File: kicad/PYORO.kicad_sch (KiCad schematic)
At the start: 69 parts, among them J1 BM06B-SRSS-TBLFSN, J2 Conn_01x04_Pin, J3 BM06B-SRSS-TBLFSN, Q1 TEFT4300, Q2 TEFT4300, Q3 TEFT4300, Q4 TEFT4300, Q5 NMOS, Q6 NMOS, Q7 NMOS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

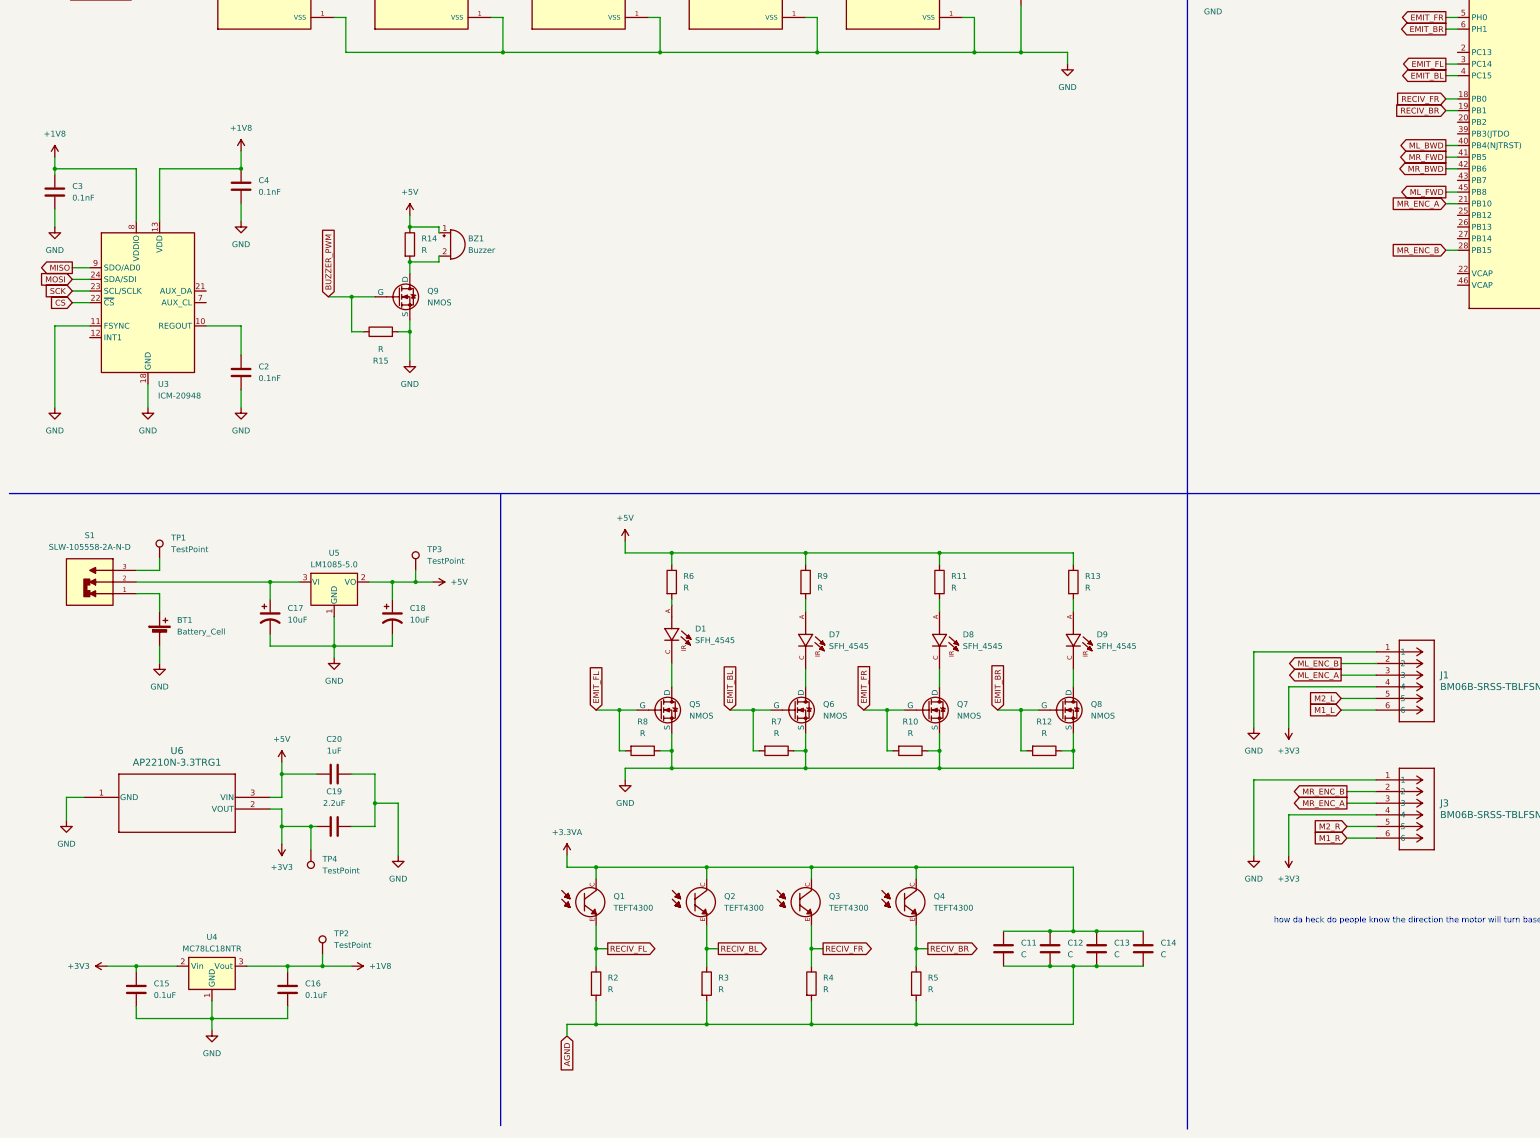
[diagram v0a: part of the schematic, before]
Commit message: Started LEDs for the extra GPIO pins
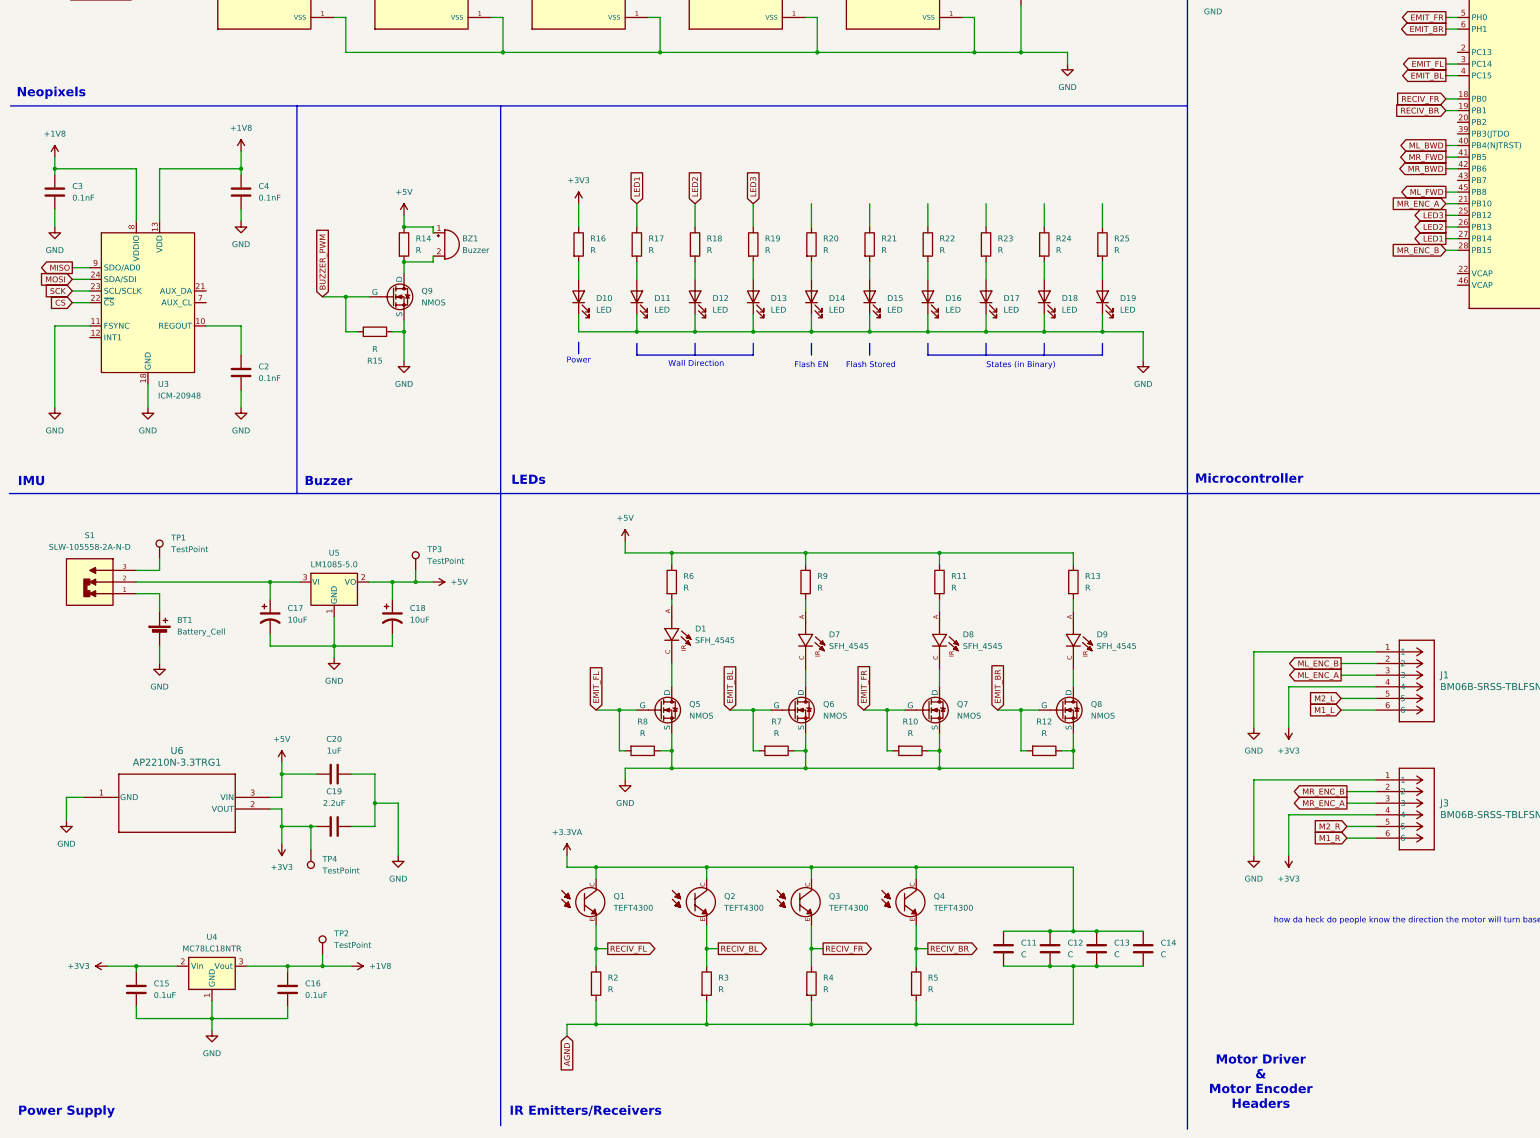
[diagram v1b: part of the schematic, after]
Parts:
- added D10, D11, D12, D13, D14, D15, D16, D17, D18, D19: LED, symbol Device:LED
- added R16, R17, R18, R19, R20, R21, R22, R23, R24, R25: R, symbol Device:R
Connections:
- net +3V3: now also R16.1
- net GND: now also D10.1 (K), D11.1 (K), D12.1 (K), D13.1 (K), D14.1 (K), D15.1 (K), D16.1 (K), D17.1 (K), D18.1 (K), D19.1 (K)
- net LED3: now reaches U1.25 (PB12)
- net LED3: now also R19.1
- net LED2: now reaches U1.26 (PB13)
- net LED2: now also R18.1
- net LED1: now reaches U1.27 (PB14)
- net LED1: now also R17.1
- new net: D17.2 (A), R23.2
- new net: D11.2 (A), R17.2
- new net: D14.2 (A), R20.2
- new net: D12.2 (A), R18.2
- new net: D18.2 (A), R24.2
- new net: D10.2 (A), R16.2
- new net: D19.2 (A), R25.2
- new net: D15.2 (A), R21.2
- new net: D13.2 (A), R19.2
- new net: D16.2 (A), R22.2
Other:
- note added: "Buzzer"
- note added: "Flash EN"
- note added: "Flash Stored"
- note added: "IMU"
- note added: "IR Emitters/Receivers"
- note added: "LEDs"
- note added: "Microcontroller"
- note added: "Motor Driver & Motor Encoder Headers"
- note added: "Neopixels"
- note added: "Power"
- note added: "Power Supply"
- note added: "States (in Binary)"
- note added: "Wall Direction"
- moved on the sheet: BZ1, C4, Q9, R14, R15

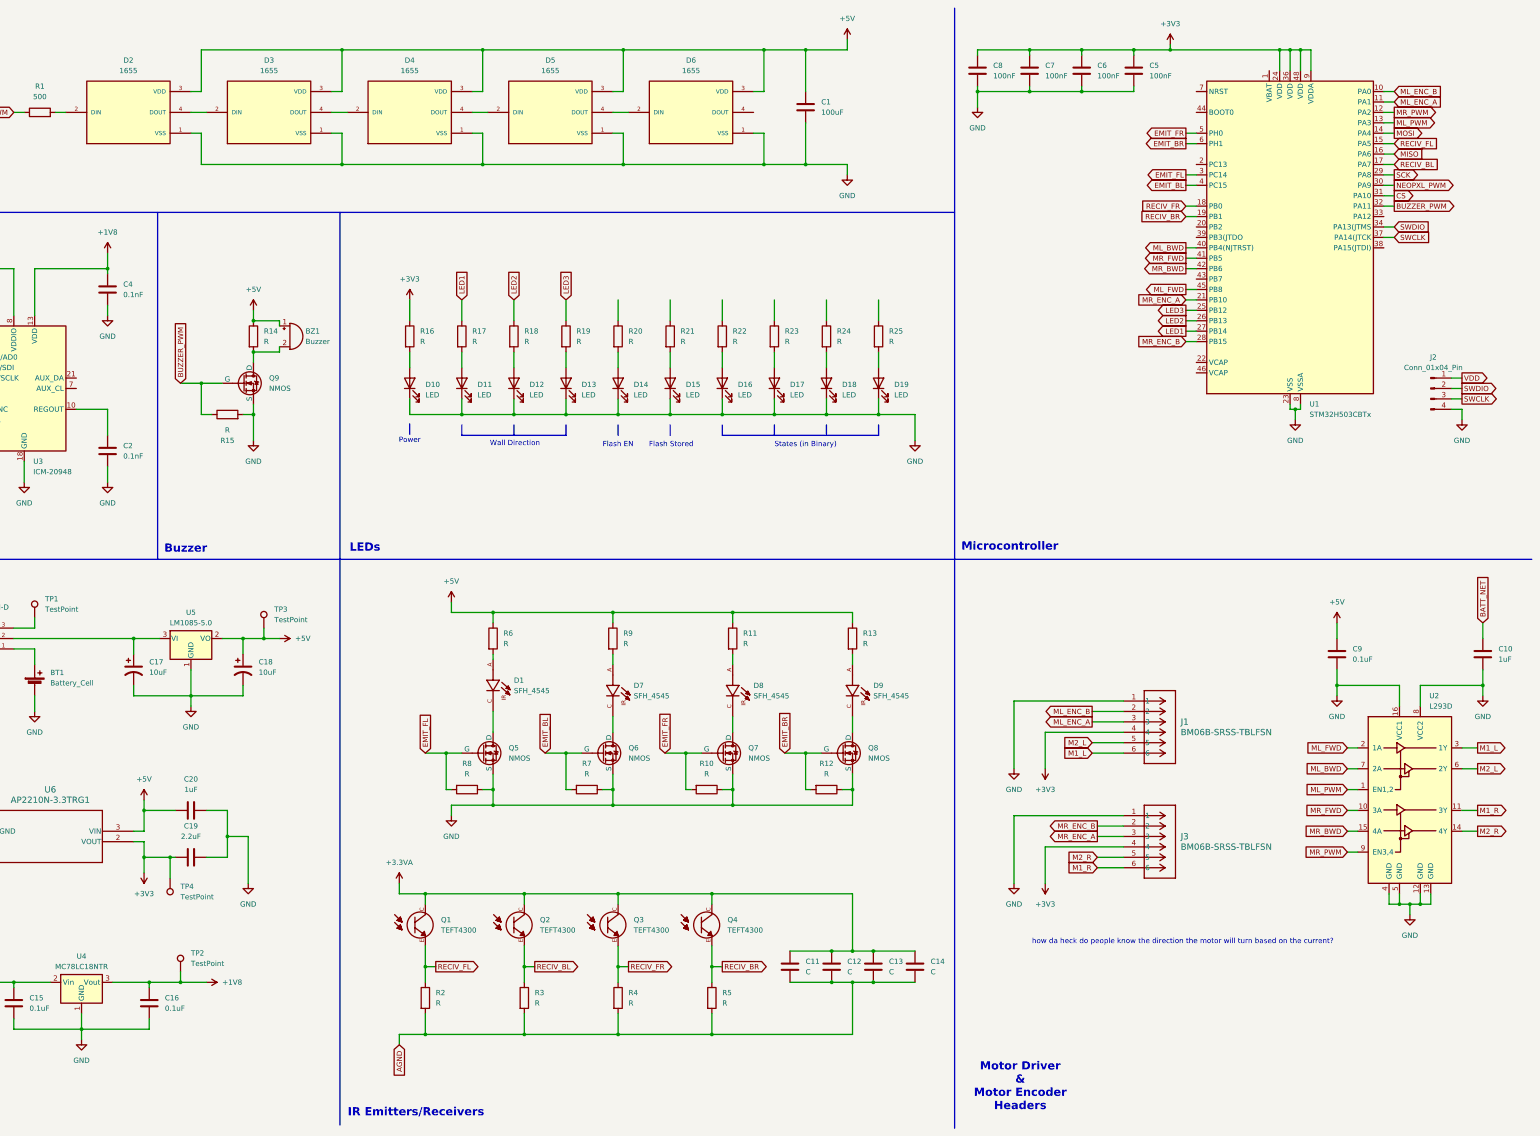
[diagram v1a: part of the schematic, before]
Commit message: Added new test points, updated missing Capacitor and Resistor values, fix MCU power supply scheme
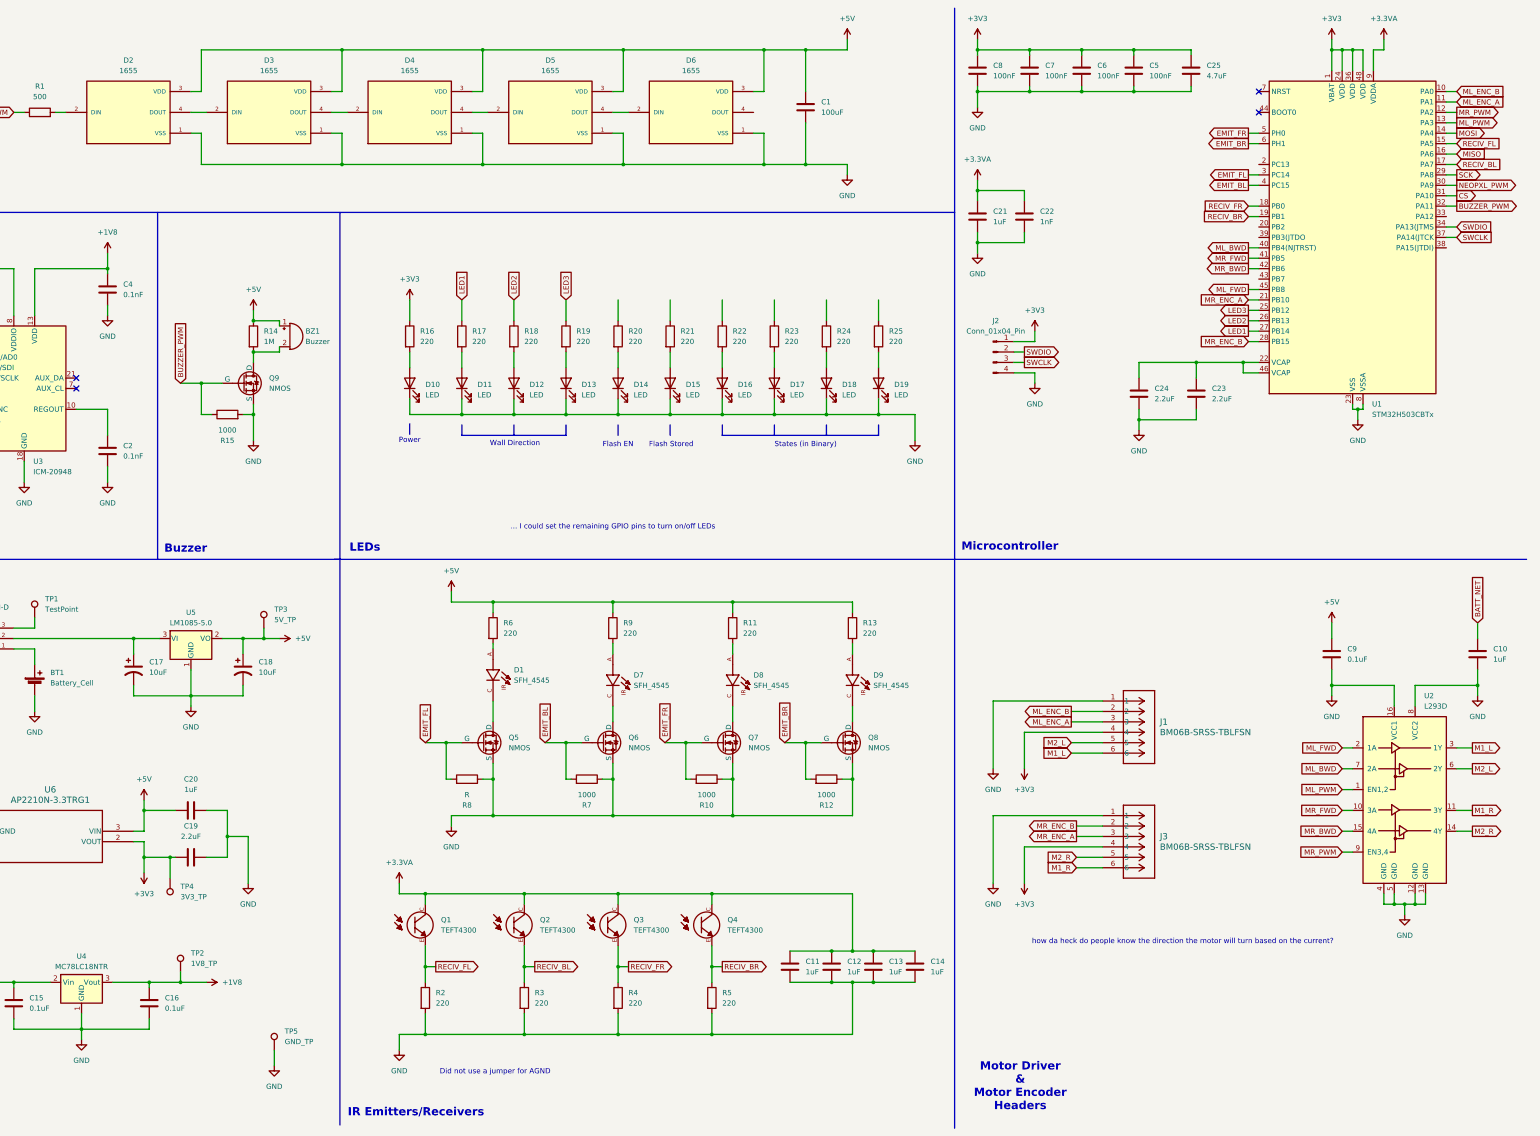
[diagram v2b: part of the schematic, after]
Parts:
- added C21: 1uF, symbol Device:C
- added C22: 1nF, symbol Device:C
- added C23, C24: 2.2uF, symbol Device:C
- added C25: 4.7uF, symbol Device:C
- added TP5: GND_TP, symbol Connector:TestPoint
- C11, C12, C13, C14: value C -> 1uF
- R10, R12, R15, R7: value R -> 1000
- R11, R13, R16, R17, R18, R19, R2, R20, R21, R22, R23, R24, R25, R3, R4, R5, R6, R9: value R -> 220
- R14: value R -> 1M
- TP2: value TestPoint -> 1V8_TP
- TP3: value TestPoint -> 5V_TP
- TP4: value TestPoint -> 3V3_TP
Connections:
- net AGND is gone; now on net GND: C11.2, C12.2, C13.2, C14.2, R2.2, R3.2, R4.2, R5.2
- net VDD is gone; now on net +3V3: J2.1 (Pin_1)
- net +3.3VA: now also U1.9 (VDDA), C21.1, C22.1
- net +3V3: now also U1.1 (VBAT), C25.1; no longer U1.9 (VDDA)
- net GND: now also C21.2, C22.2, C23.2, C24.2, C25.2, TP5.1
- net at U1.22 (VCAP): now also U1.46 (VCAP), C23.1, C24.1
- no-connect marks 0 -> 4
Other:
- note added: "... I could set the remaining GPIO pins to turn on/off LEDs"
- note added: "Did not use a jumper for AGND"
- title: (none) -> Pyoro Schematic
- moved on the sheet: C10, C9, D1, D7, D8, D9, J1, J2, J3, Q5, Q6, Q7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
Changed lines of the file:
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@@
 	(generator_version "8.0")
 	(paper "A3")
+	(title_block
+		(title "Pyoro Schematic")
+		(date "8/7/2025")
+		(rev "1.0")
+	)

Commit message: Added Filtering for 3.3VA
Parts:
- added C26: C, symbol Device:C
- added R26: R, symbol Device:R
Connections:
- net +3.3VA: now also C26.1, R26.2
- net +3V3: now also R26.1
- net GND: now also C26.2
- no-connect marks 4 -> 5
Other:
- moved on the sheet: C15, C16, C19, C20, TP2, TP4, TP5, U4, U6

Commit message: Fixed spelling errors
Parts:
- C2, C3, C4: value 0.1nF -> 0.1uF
- C22: value 1nF -> 100nF
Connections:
- net +3V3: now also C19.2; no longer C19.1
- net GND: now also C19.1; no longer C19.2
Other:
- moved on the sheet: C15, C16, C19, C26, R26, TP2, TP4, TP5, U4

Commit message: Converted capacitor units
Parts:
- C22, C5, C6, C7, C8: value 100nF -> 0.1uF

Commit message: Added new symbols for silkscreen and IMU backup
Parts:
- added C27: 4.7uF, symbol Device:C
- added FSP-1: ~, Package_QFP:LQFP-48_7x7mm_P0.5mm, symbol FSP201:FSP201
- R8: value R -> 1000
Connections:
- net +3V3: now also FSP-1.42 (AVCC0), FSP-1.45 (P101/VREFH0), FSP-1.9 (VCC)
- net +5V: now also U2.16 (VCC1)
- net BATT_NET: now also U2.8 (VCC2)
- net GND: now also C27.2, FSP-1.31 (VSS), FSP-1.43 (AVSS0), FSP-1.44 (P011/VREFL0), FSP-1.6 (VSS); no longer U2.16 (VCC1), U2.8 (VCC2)
- new net: C27.1, FSP-1.3 (VCL)
